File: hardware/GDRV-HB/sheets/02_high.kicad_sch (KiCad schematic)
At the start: 62 parts, among them J201 TSW-104-07-G-S, J202 TSW-101-07-G-S, Q201 2N7002BK, Q202 PMV30ENEAR, Q203 MMBT3904,215, Q204 MMBT3906,215, U201 SN74LVC1G17DBVR, U202 UCC14241QDWNRQ1, U203 NSI6651ASC-Q1SWR

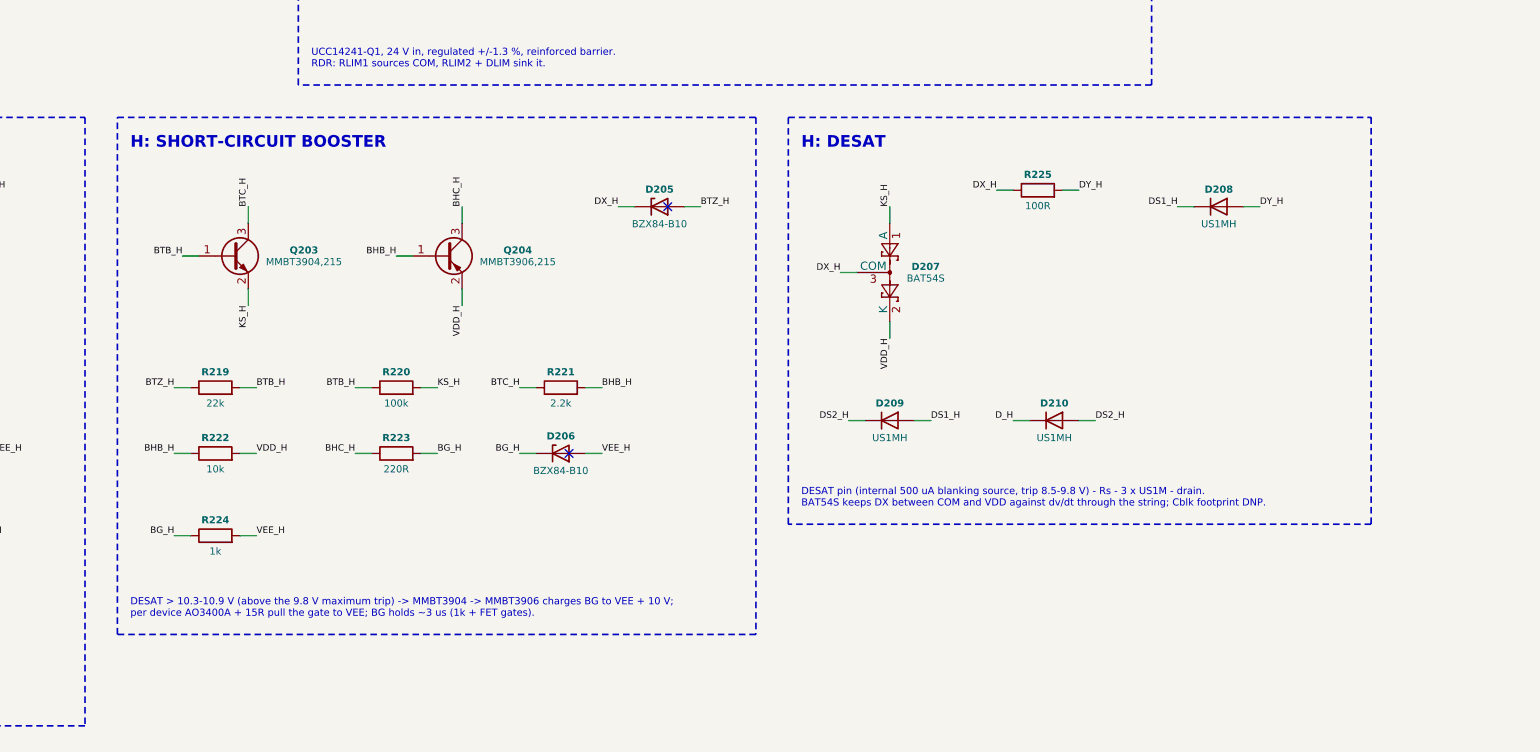
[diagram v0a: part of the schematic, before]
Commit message: Resolve the independent PCM review of 033d8d8 (PCM-01..27): verify, classify, fix at the root (D-065..D-072)
Register gen/data/review_pcm.csv: 27 findings, each verified before a change - 21 Confirmed, 2 Firmware
Handled, 3 Improvement Recommended, 1 Not Applicable; 20 closed, 7 open with their closing path.

PV family (D-065, D-072): the 45 A port rating no longer clamps the inductor current in the near-unity
band (inductor rating 47.7 A there; 550/550 V 73.3 kW; rated power from 562 V); control model re-based on
the drawn boards with a published delivered-power envelope per product and direction; leg commutation
re-run on the drawn Jianghai capacitors (1374 V worst vs 1445 V); comparator common-mode term in every
trip band (window 67.9-80.5 A, the 1.10 margin rule missed by 0.58 A and left open; firmware OV derived
from the drawn band, 1034 V); one fan-supply contract; cold-start passive-power restriction modelled;
port A interface declared; aux pull-in and retry rules.

PCS-P125 (D-066, D-067): control study sim/pcs_control.py (PR current loop 1750 Hz, PM >= 48.7 deg to
SCR 5 with the passive damping branch, PLL, DC-link loop, grid forming, state machine); DC-link inventory
409.4 uF with bleeders, precharge rating and the 15 min label re-derived; upper-half limit in firmware;
P-Q-Vdc-Vac envelope (AC-02's 600 V full-load figure not reachable at a +15 % grid: owner's decision);
R_DS(on) acceptance rule for the six paralleled devices; DESAT string 3 -> 2 diodes (band 6.41-9.37 V);
fuse-contactor coordination bands and installation requirements; phase-current sensor frozen to Sinomags
STK-250HO/4 and the control-board ladders re-valued; Al2O3 pad text.

DAB-D60 (D-068): study vs drawn-board identity made explicit; short-circuit chain corrected (energy-
equivalent 0.99 x the assumed withstand; release block t_SC >= 2.22 us / E_SC >= 2.18 J); admitted map
follows the 1200 V deck envelope (900-950 V rows derated until a double-pulse test); zero/light-load policy;
0.41 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
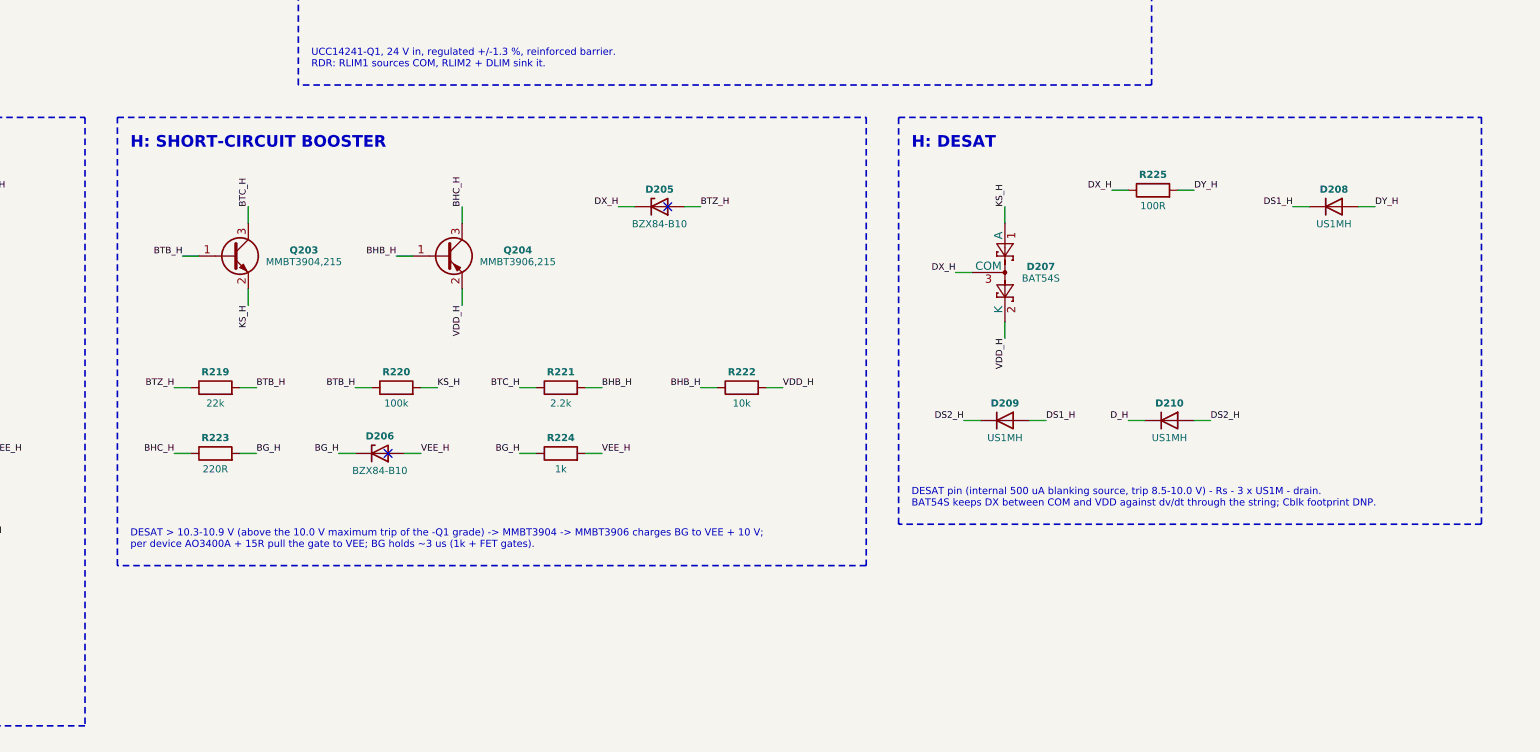
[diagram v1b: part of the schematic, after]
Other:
- note added: "DESAT > 10.3-10.9 V (above the 10.0 V maximum trip of the -Q1 grade) -> MMBT3904 -> MMBT3906 charges BG to VEE + 10 V; per device AO3400A + 15R pull the gate to VEE; BG holds ~3 us (1k + FET gates)."
- note added: "DESAT pin (internal 500 uA blanking source, trip 8.5-10.0 V) - Rs - 3 x US1M - drain. BAT54S keeps DX between COM and VDD against dv/dt through the string; Cblk footprint DNP."
- note removed: "DESAT > 10.3-10.9 V (above the 9.8 V maximum trip) -> MMBT3904 -> MMBT3906 charges BG to VEE + 10 V; per device AO3400A + 15R pull the gate to VEE; BG holds ~3 us (1k + FET gates)."
- note removed: "DESAT pin (internal 500 uA blanking source, trip 8.5-9.8 V) - Rs - 3 x US1M - drain. BAT54S keeps DX between COM and VDD against dv/dt through the string; Cblk footprint DNP."
- moved on the sheet: D206, D207, D208, D209, D210, R222, R223, R224, R225

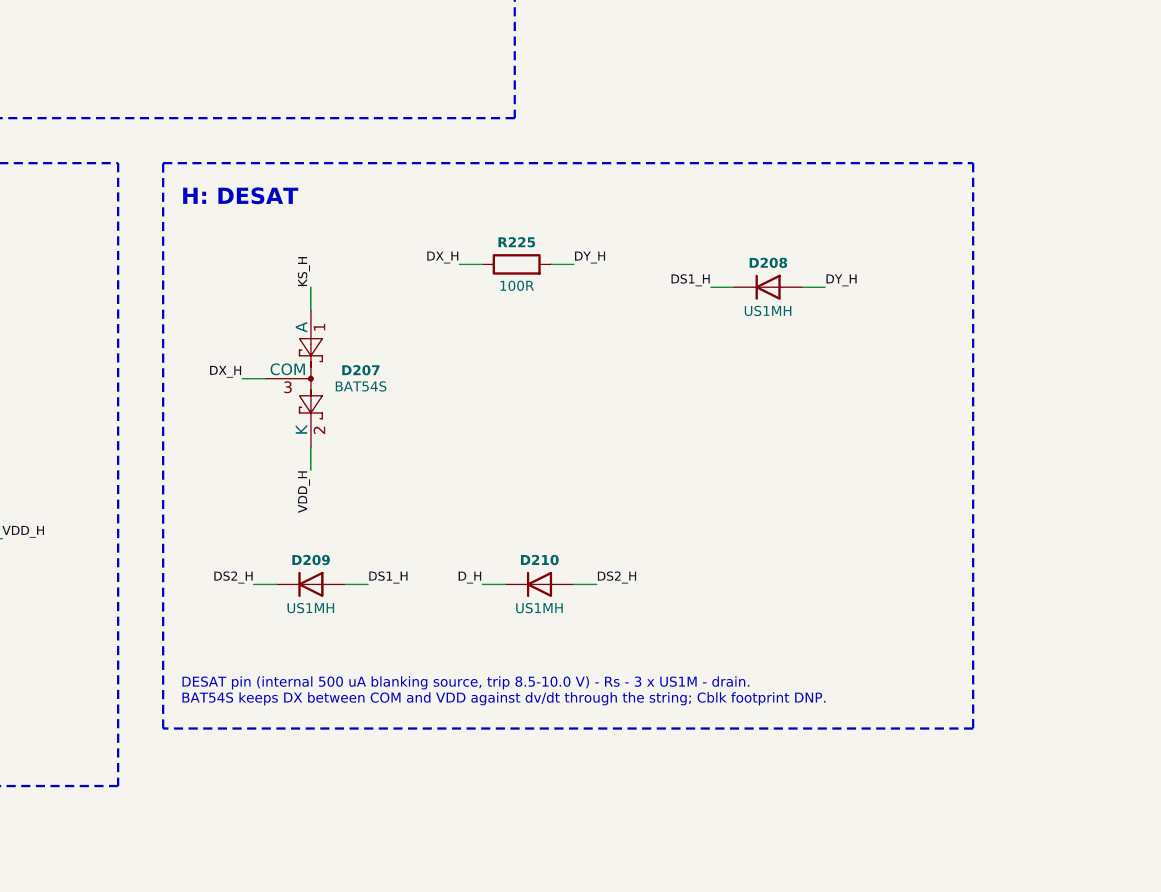
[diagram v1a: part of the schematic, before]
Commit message: Respond to the independent economical re-check R4 of 845131d (D-081): DESAT string re-rated to 1300 V diodes, cable-aware DC-bus window enforced, off-grid envelope stated as declared capability, inverter cold rating -10 C, grade-B rating stated, magnetics RFQ index
- Register gen/data/review_r4.csv: 12 decision areas closed (3 Confirmed, 4 Already Fixed, 3 Improvement Recommended, 2 Not Applicable)
- E01: the DESAT sense string sees the whole DC link (static envelope 1130 V) on an off switch; 2 x Vishay BYG23T-M3/TR (1300 V)
  per channel on both presets, each diode blocking the envelope alone; PCS window unchanged, PV preset 3 -> 2 diodes; grade
  tables identical; +0.96 to +2.12 USD per module at 5k; datasheet, prices, ledger rows, insulation table
- E04: inter-module cable in the coupled PCS/PV bus model (+28 V); product rule default set point 750 V (755 V four-wire mode A),
  782 V firmware clamp in the PV module, PCS refuses an island start above 791 V, 909 V recorded as model validity; harness contract
- E06: AC-04 reworded as the module's declared output capability with the release sequence (grid-following first)
- E11: PCS cold-start passive table modelled; rating full operation from -10 C inlet (AC-02 amended by delegation), cold fan RFQ open
- E05: grade-B rating 124.57 kW at PF 1 stated; E12: docs/requirements/RFQ-MAGNETICS.md (ten RFQs); the port CM ring's catalog
  entry set to the flat-permeability grade and the aux transformer's thermal test to the 94.2 W rating
- All 15 boards, BOMs, costs, comparisons (PV 2/24/3/5/0, PCS 2/38/4/9/0), audits (pin 192/0/55, insulation 98 known) and figures
  regenerated; README, guide 01-13, INSTALLATION.md (77 rows), decisions mirror and the registers updated

Co-Authored-By: Claude Fable 5.1 <noreply@anthropic.com>
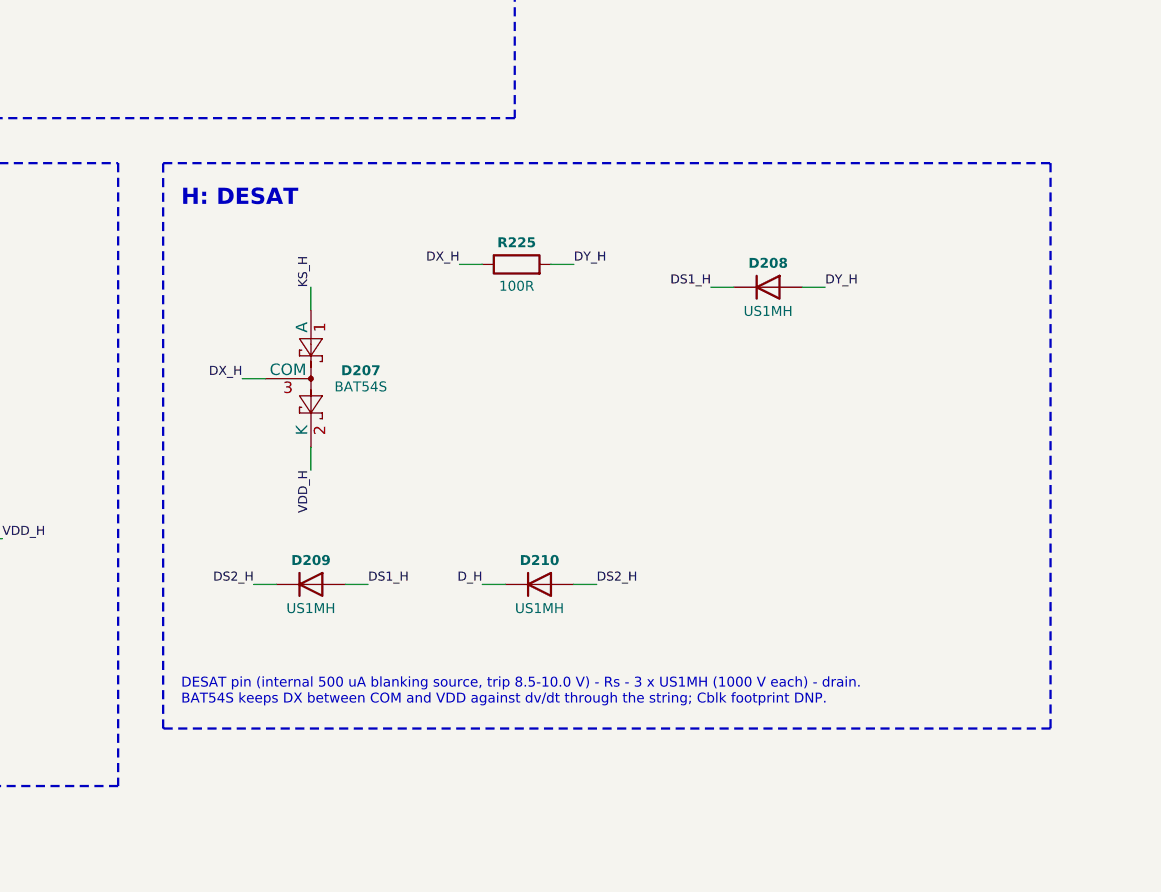
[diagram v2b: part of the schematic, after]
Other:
- note added: "DESAT pin (internal 500 uA blanking source, trip 8.5-10.0 V) - Rs - 3 x US1MH (1000 V each) - drain. BAT54S keeps DX between COM and VDD against dv/dt through the string; Cblk footprint DNP."
- note removed: "DESAT pin (internal 500 uA blanking source, trip 8.5-10.0 V) - Rs - 3 x US1M - drain. BAT54S keeps DX between COM and VDD against dv/dt through the string; Cblk footprint DNP."
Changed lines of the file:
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@@
 	(rectangle
 		(start 278.22 138.61)
-		(end 368.22 201.43)
+		(end 376.82 201.43)
 		(stroke
 			(width 0.254)
@@
 		)
 	)
-	(text "DESAT pin (internal 500 uA blanking source, trip 8.5-10.0 V) - Rs - 3 x US1M - drain.\nBAT54S keeps DX between COM and VDD against dv/dt through the string; Cblk footprint DNP."
+	(text "DESAT pin (internal 500 uA blanking source, trip 8.5-10.0 V) - Rs - 3 x US1MH (1000 V each) - drain.\nBAT54S keeps DX between COM and VDD against dv/dt through the string; Cblk footprint DNP."
 		(exclude_from_sim no)
 		(at 280.22 198.928 0)
